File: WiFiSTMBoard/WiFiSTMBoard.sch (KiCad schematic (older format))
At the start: 22 parts

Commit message: added input
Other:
- note added: "MICROCONTROLLER"
- moved on the sheet: C?, D?, J?, L?, R?, SW?, U?, Y?

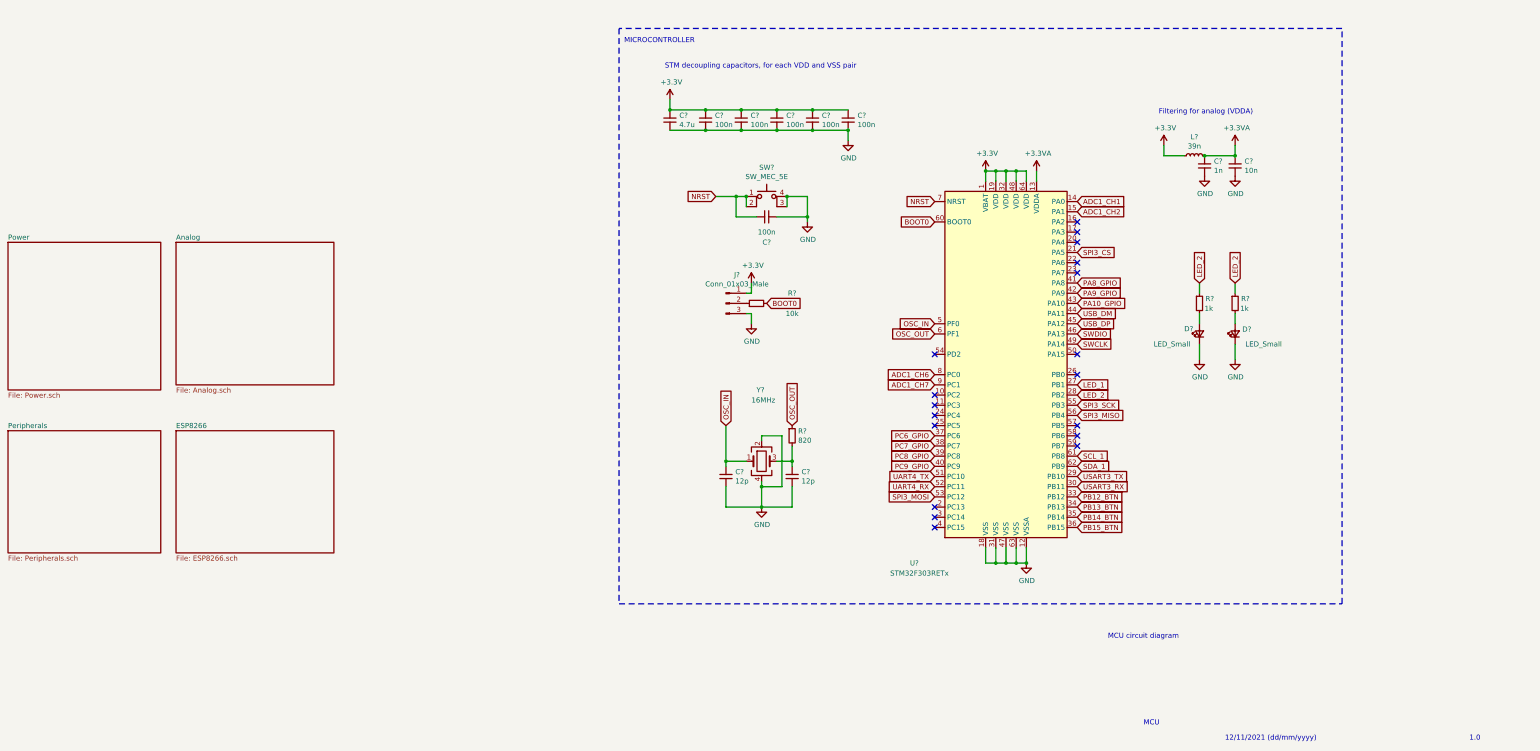
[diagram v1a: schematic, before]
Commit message: added esp8266
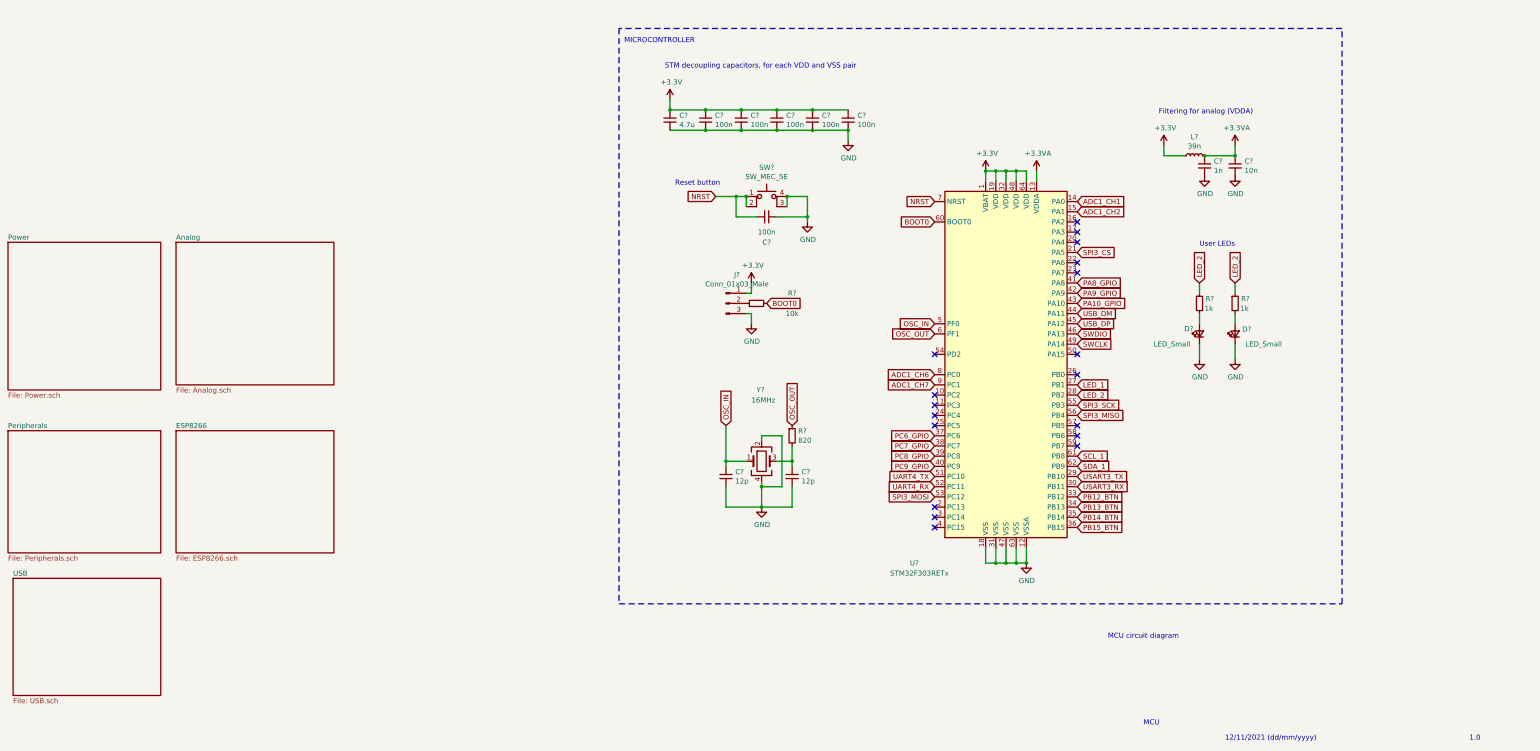
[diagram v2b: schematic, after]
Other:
- note added: "Reset button"
- note added: "User LEDs"
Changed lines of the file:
@@
 $Descr A4 11693 8268
 encoding utf-8
-Sheet 1 5
+Sheet 1 6
 Title ""
 Date ""
@@
 Text Notes 2250 800  0    50   ~ 0
 MICROCONTROLLER
+$Sheet
+S -3750 6050 1450 1150
+U 6195631A
+F0 "USB" 50
+F1 "USB.sch" 50
+$EndSheet
+Text Notes 7900 2800 0    50   ~ 0
+User LEDs
+Text Notes 2750 2200 0    50   ~ 0
+Reset button
 $EndSCHEMATC

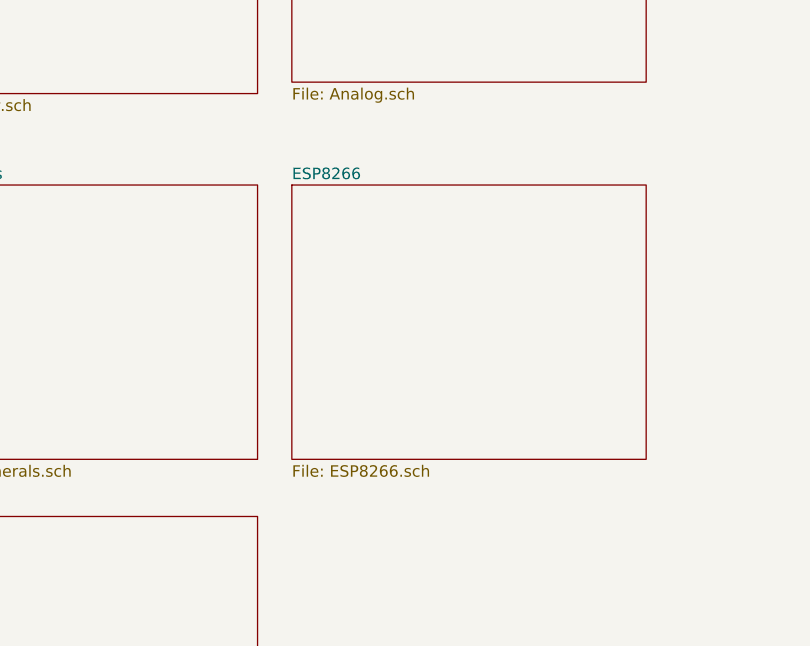
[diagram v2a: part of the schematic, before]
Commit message: removed esp8266 diagram, added ch3040 diagram
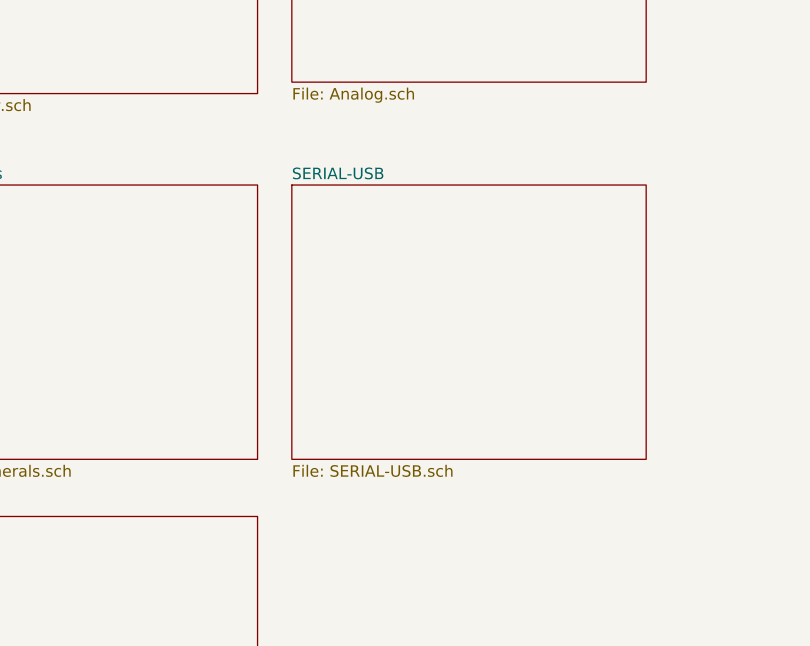
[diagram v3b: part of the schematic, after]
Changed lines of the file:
@@
 S -2150 4600 1550 1200
 U 61A77DC4
-F0 "ESP8266" 50
-F1 "ESP8266.sch" 50
+F0 "SERIAL-USB" 50
+F1 "SERIAL-USB.sch" 50
 $EndSheet
 NoConn ~ 5300 3850

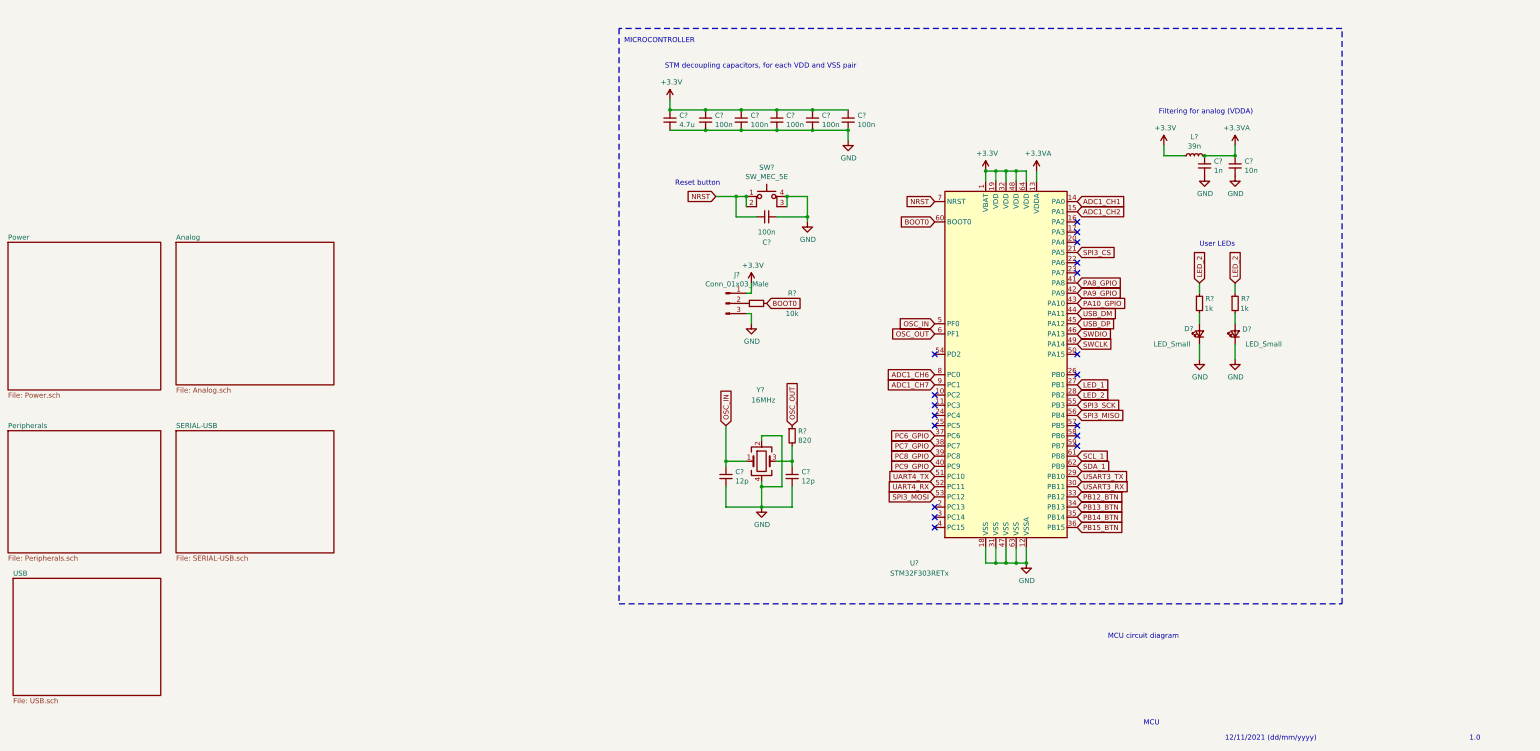
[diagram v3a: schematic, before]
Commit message: finished serial circuit
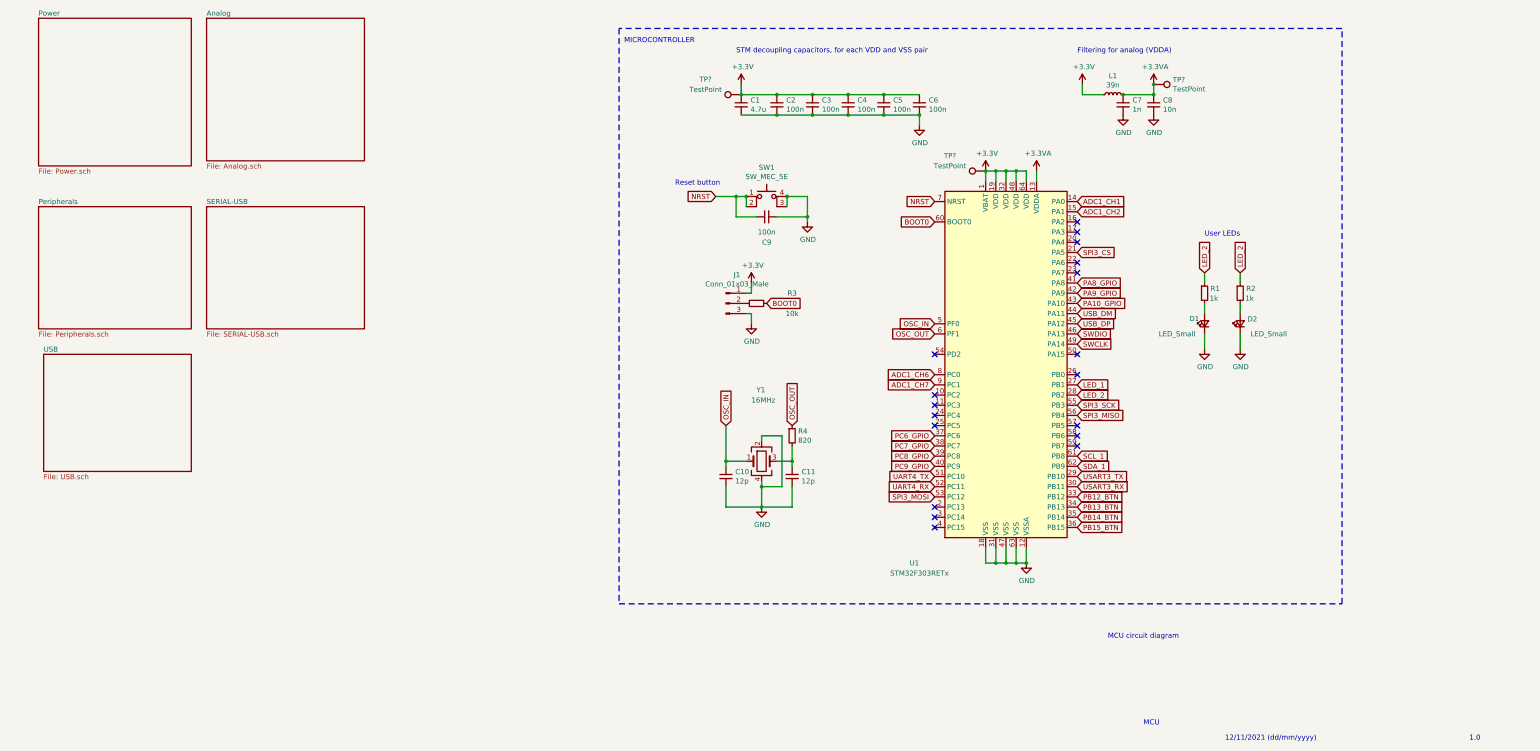
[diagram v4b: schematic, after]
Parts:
- added TP? (x3): TestPoint, symbol Connector:TestPoint
- gave numbers to parts that had none: 22
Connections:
- net +3.3VA: now also TP?.1
- net +3V3: now also TP?.1, TP?.1
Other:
- moved on the sheet: C1, C2, C3, C4, C5, C6, C7, C8, D1, D2, L1, R1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

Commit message: starting PCB layout
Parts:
- removed SW1: SW_MEC_5E, symbol Switch:SW_MEC_5E
- added H1, H2, H3, H4: MountingHole_Pad, MountingHole:MountingHole_2.2mm_M2_Pad_Via, symbol Mechanical:MountingHole_Pad
- added SW1: SW_Push_Dual_x2, Button_Switch_SMD:SW_Push_1P1T_NO_6x6mm_H9.5mm, symbol Switch:SW_Push_Dual_x2
- C1: renamed from C7; footprint (none) -> Capacitor_SMD:C_0603_1608Metric
- C10, C11: footprint (none) -> Capacitor_SMD:C_0402_1005Metric
- C2: renamed from C8; footprint (none) -> Capacitor_SMD:C_0603_1608Metric
- C3: renamed from C1; footprint (none) -> Capacitor_SMD:C_0603_1608Metric
- C4: renamed from C2; footprint (none) -> Capacitor_SMD:C_0603_1608Metric
- C5: renamed from C3; footprint (none) -> Capacitor_SMD:C_0603_1608Metric
- C6: renamed from C4; footprint (none) -> Capacitor_SMD:C_0603_1608Metric
- C7: renamed from C5; footprint (none) -> Capacitor_SMD:C_0603_1608Metric
- C8: renamed from C6; footprint (none) -> Capacitor_SMD:C_0603_1608Metric
- C9: footprint (none) -> Capacitor_SMD:C_0603_1608Metric
- D1, D2: footprint (none) -> LED_SMD:LED_1206_3216Metric
- J1: footprint (none) -> Connector_PinHeader_2.54mm:PinHeader_1x03_P2.54mm_Vertical
- L1: footprint (none) -> Inductor_SMD:L_0603_1608Metric
- R1, R2: footprint (none) -> Resistor_SMD:R_1206_3216Metric
- R3: footprint (none) -> Resistor_SMD:R_0805_2012Metric
- R4: footprint (none) -> Resistor_SMD:R_0603_1608Metric
- TP1, TP2, TP3: renamed from TP?; footprint (none) -> TestPoint:TestPoint_Pad_D2.0mm
- Y1: footprint (none) -> Crystal:Crystal_SMD_3225-4Pin_3.2x2.5mm
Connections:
- net GND: now also H1.1, H2.1, H3.1, H4.1, SW1.2 (D)
- net NRST: now also SW1.1 (C)
- net PA4_GPIO: now reaches U1.20 (PA4)
- net PA6_GPIO: now reaches U1.22 (PA6)
- net PA7_GPIO: now reaches U1.23 (PA7)
- net SCL_1 renamed SCL
- net SDA_1 renamed SDA
- net SPI3_CS renamed PA5_GPIO
- net SPI3_MISO: no longer names the net of U1.56 (PB4)
- net SPI3_MOSI: no longer names the net of U1.53 (PC12)
- net SPI3_SCK renamed SWO
- no-connect marks 18 -> 16
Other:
- note added: "Mounting holes"
- moved on the sheet: C10, C11, C3, C4, C5, C6, C7, C8, J1, R3, R4, TP2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

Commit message: .
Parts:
- removed C8: 100n, Capacitor_SMD:C_0603_1608Metric, symbol Device:C_Small
- removed TP2: TestPoint, TestPoint:TestPoint_Pad_D2.0mm, symbol Connector:TestPoint
- removed U1: STM32F303RETx, Package_QFP:LQFP-64_10x10mm_P0.5mm, symbol MCU_ST_STM32F3:STM32F303RETx
- added U1: STM32F302C8Tx, Package_QFP:LQFP-48_7x7mm_P0.5mm, symbol MCU_ST_STM32F3:STM32F302C8Tx
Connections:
- net +3.3VA: now also U1.9 (VDDA)
- net +3V3: now also U1.1 (VBAT), U1.24 (VDD), U1.36 (VDD), U1.48 (VDD)
- net ADC1_CH1: now also U1.10 (PA0)
- net ADC1_CH2: now also U1.11 (PA1)
- net BOOT0: now also U1.44 (BOOT0)
- net GND: now also U1.23 (VSS), U1.35 (VSS), U1.47 (VSS), U1.8 (VSSA)
- net LED_1: now also R1.1, U1.19 (PB1)
- net LED_2: now also U1.18 (PB0); no longer R1.1
- net NRST: now also U1.7 (NRST)
- net OSC_IN: now also U1.5 (PF0)
- net OSC_OUT: now also U1.6 (PF1)
- net SCL: now also U1.45 (PB8)
- net SDA: now also U1.46 (PB9)
- net SWCLK: now also U1.37 (PA14)
- net SWDIO: now also U1.34 (PA13)
- net SWO: now also U1.39 (PB3)
- net USART3_RX: now also U1.22 (PB11)
- net USART3_TX: now also U1.21 (PB10)
- net USB_DM: now also U1.32 (PA11)
- net USB_DP: now also U1.33 (PA12)
- new net ADC1_CH3: U1.12 (PA2)
- new net PA3_BTN: U1.13 (PA3)
- new net PA4_BTN: U1.14 (PA4)
- new net PA5_BTN: U1.15 (PA5)
- new net PA6_BTN: U1.16 (PA6)
- new net PA7: U1.17 (PA7)
- new net PA8: U1.29 (PA8)
- new net PB12: U1.25 (PB12)
- new net PB13: U1.26 (PB13)
- new net PB14: U1.27 (PB14)
- new net PB15: U1.28 (PB15)
- new net PB2_GPIO: U1.20 (PB2)
- new net PB4_GPIO: U1.40 (PB4)
- new net PB5_GPIO: U1.41 (PB5)
- new net PB6_GPIO: U1.42 (PB6)
- new net PB7_GPIO: U1.43 (PB7)
- new net PC13: U1.2 (PC13)
- new net PC14: U1.3 (PC14)
- new net PC15: U1.4 (PC15)
- new net UART1_RX: U1.31 (PA10)
- new net UART1_TX: U1.30 (PA9)
- no-connect marks 16 -> 1
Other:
- moved on the sheet: TP3
